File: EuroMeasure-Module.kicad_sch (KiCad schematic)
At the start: 0 parts

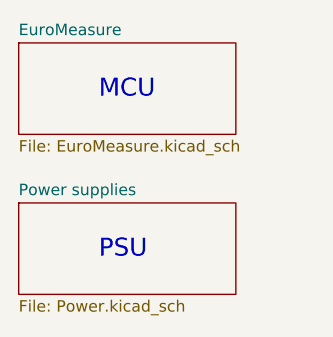
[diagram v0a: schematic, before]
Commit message: Updated PCB to current standards
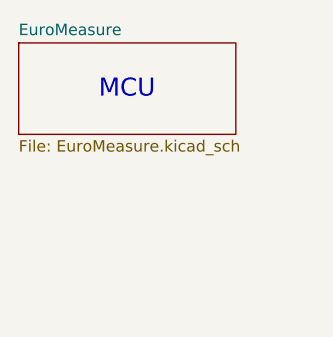
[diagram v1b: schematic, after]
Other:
- removed sheet Power supplies
- note removed: "PSU"
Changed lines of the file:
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@@
-    (effects (font (size 2 2)) (justify left bottom))
-  )
-  (text "PSU" (at 262.89 43.18 0)
     (effects (font (size 2 2)) (justify left bottom))
   )
@@
       )
     )
-  )
-  (sheet (at 254 36.83) (size 24.13 10.16) (fields_autoplaced)
-    (stroke (width 0.1524) (type solid))
-    (fill (color 0 0 0 0.0000))
-    (property "Sheetname" "Power supplies" (at 254 36.1184 0)
-      (effects (font (size 1.27 1.27)) (justify left bottom))
-    )
-    (property "Sheetfile" "Power.kicad_sch" (at 254 47.5746 0)
-      (effects (font (size 1.27 1.27)) (justify left top))
-    )
-    (instances
-      (project "EuroMeasure-Module"
-        (path "/9c84a828-ebcc-4f88-b5cc-11be4f5044ad" (page "7"))
-      )
-    )
